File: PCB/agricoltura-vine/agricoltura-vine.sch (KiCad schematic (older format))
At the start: 0 parts

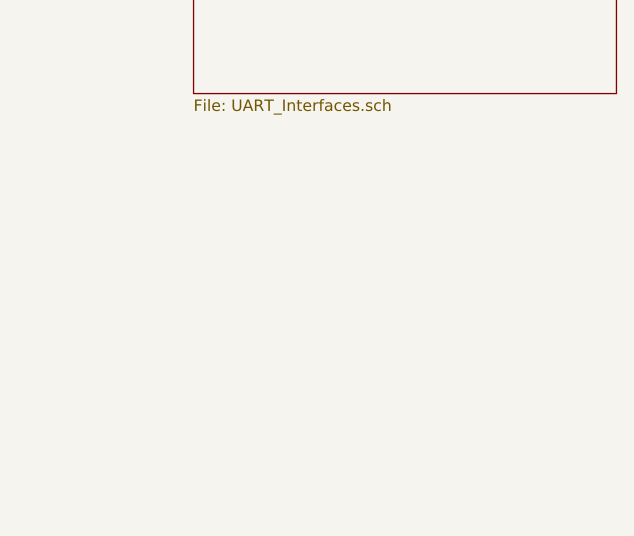
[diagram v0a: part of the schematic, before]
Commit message: 5V Logic, Connector swap, and I2C refactor
Added 5V IO logic, changed connectors over to grove style SMT, I2C refactored to use 8x mux instead fo two 4x mux.
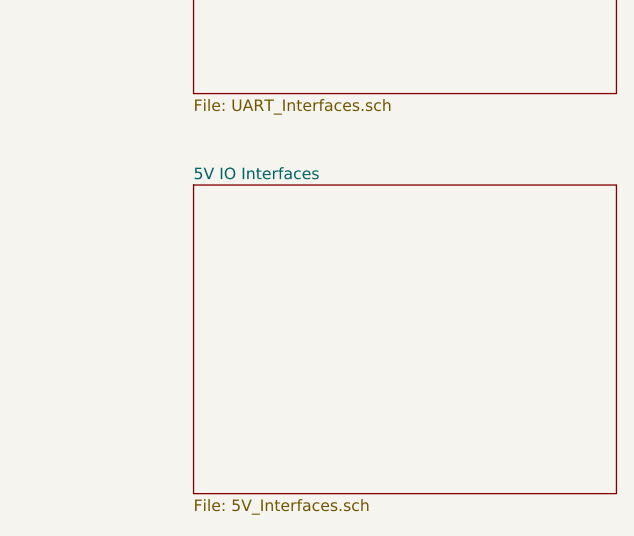
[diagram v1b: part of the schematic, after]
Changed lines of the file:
@@
 $Descr A4 11693 8268
 encoding utf-8
-Sheet 1 6
+Sheet 1 7
 Title ""
 Date ""
@@
 F1 "RS485_Interface.sch" 50
 $EndSheet
+$Sheet
+S 7550 4550 1850 1350
+U 5EF943A9
+F0 "5V IO Interfaces" 50
+F1 "5V_Interfaces.sch" 50
+$EndSheet
 $EndSCHEMATC

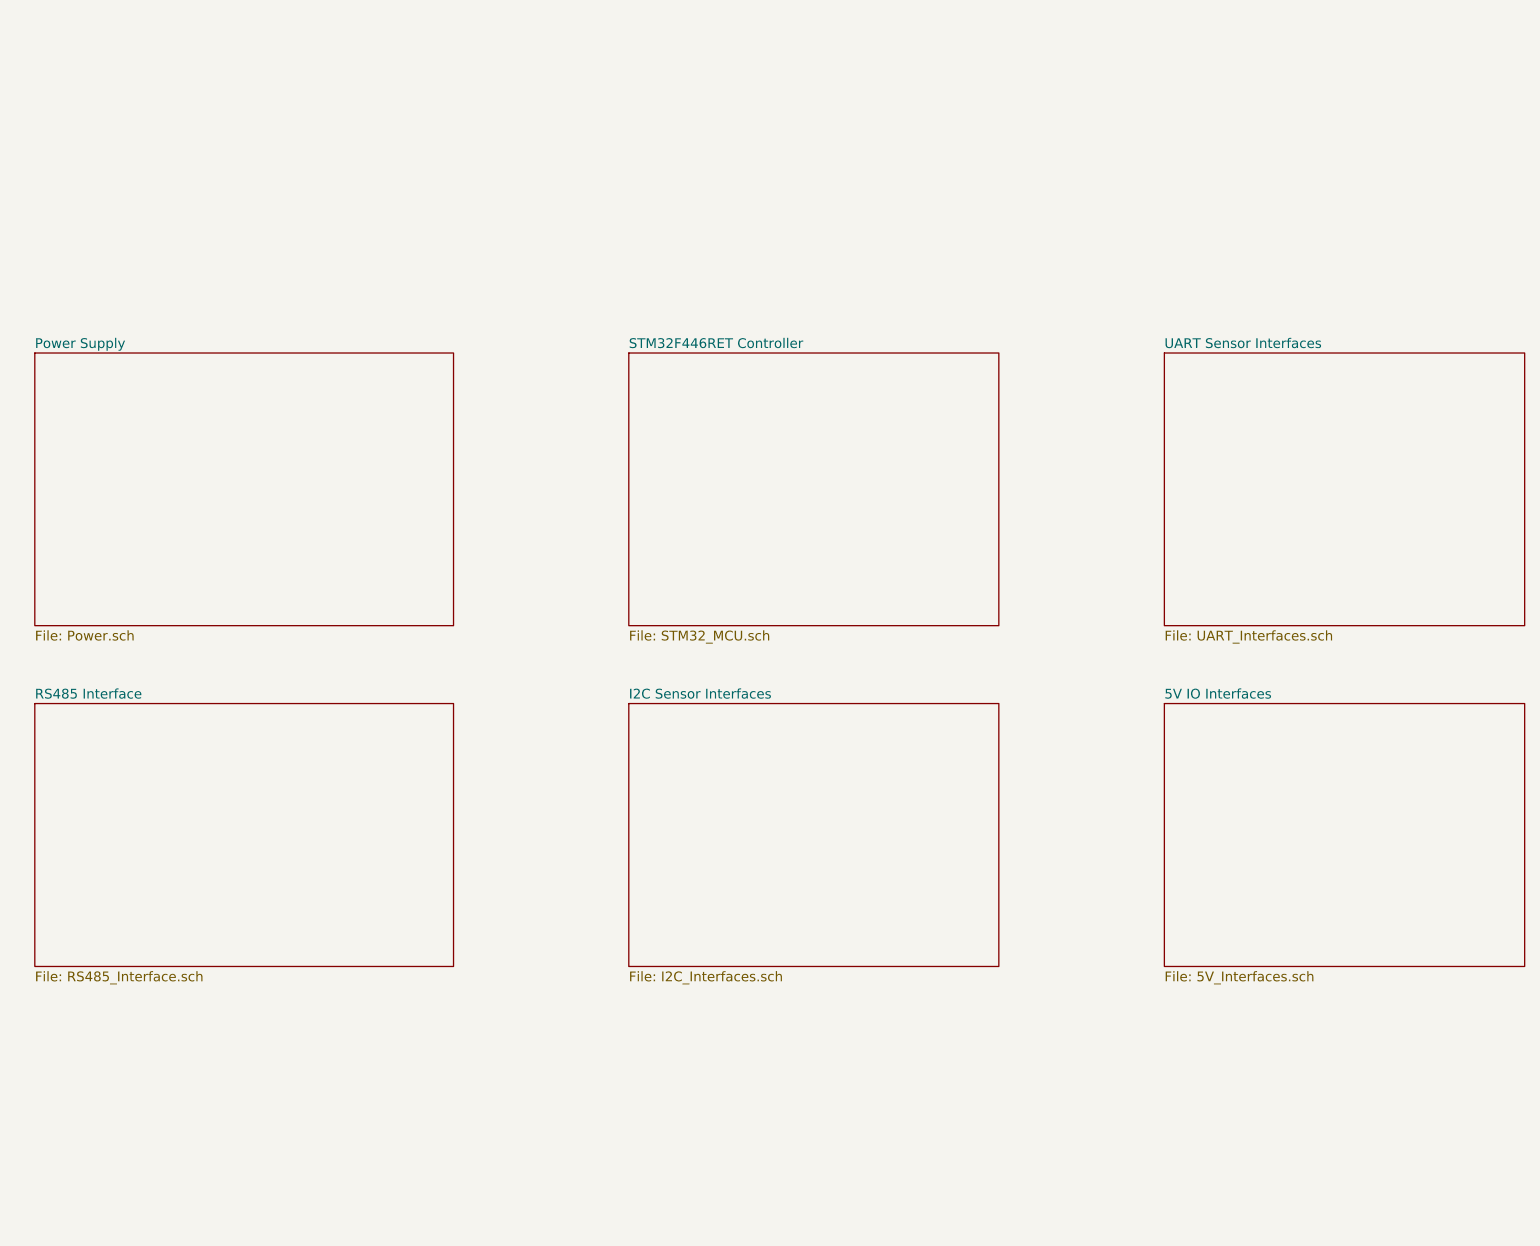
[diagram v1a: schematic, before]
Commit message: Schematic Pass 1
All subsystem schematics are completed in their first pass, some features scaled back to make design more practical.
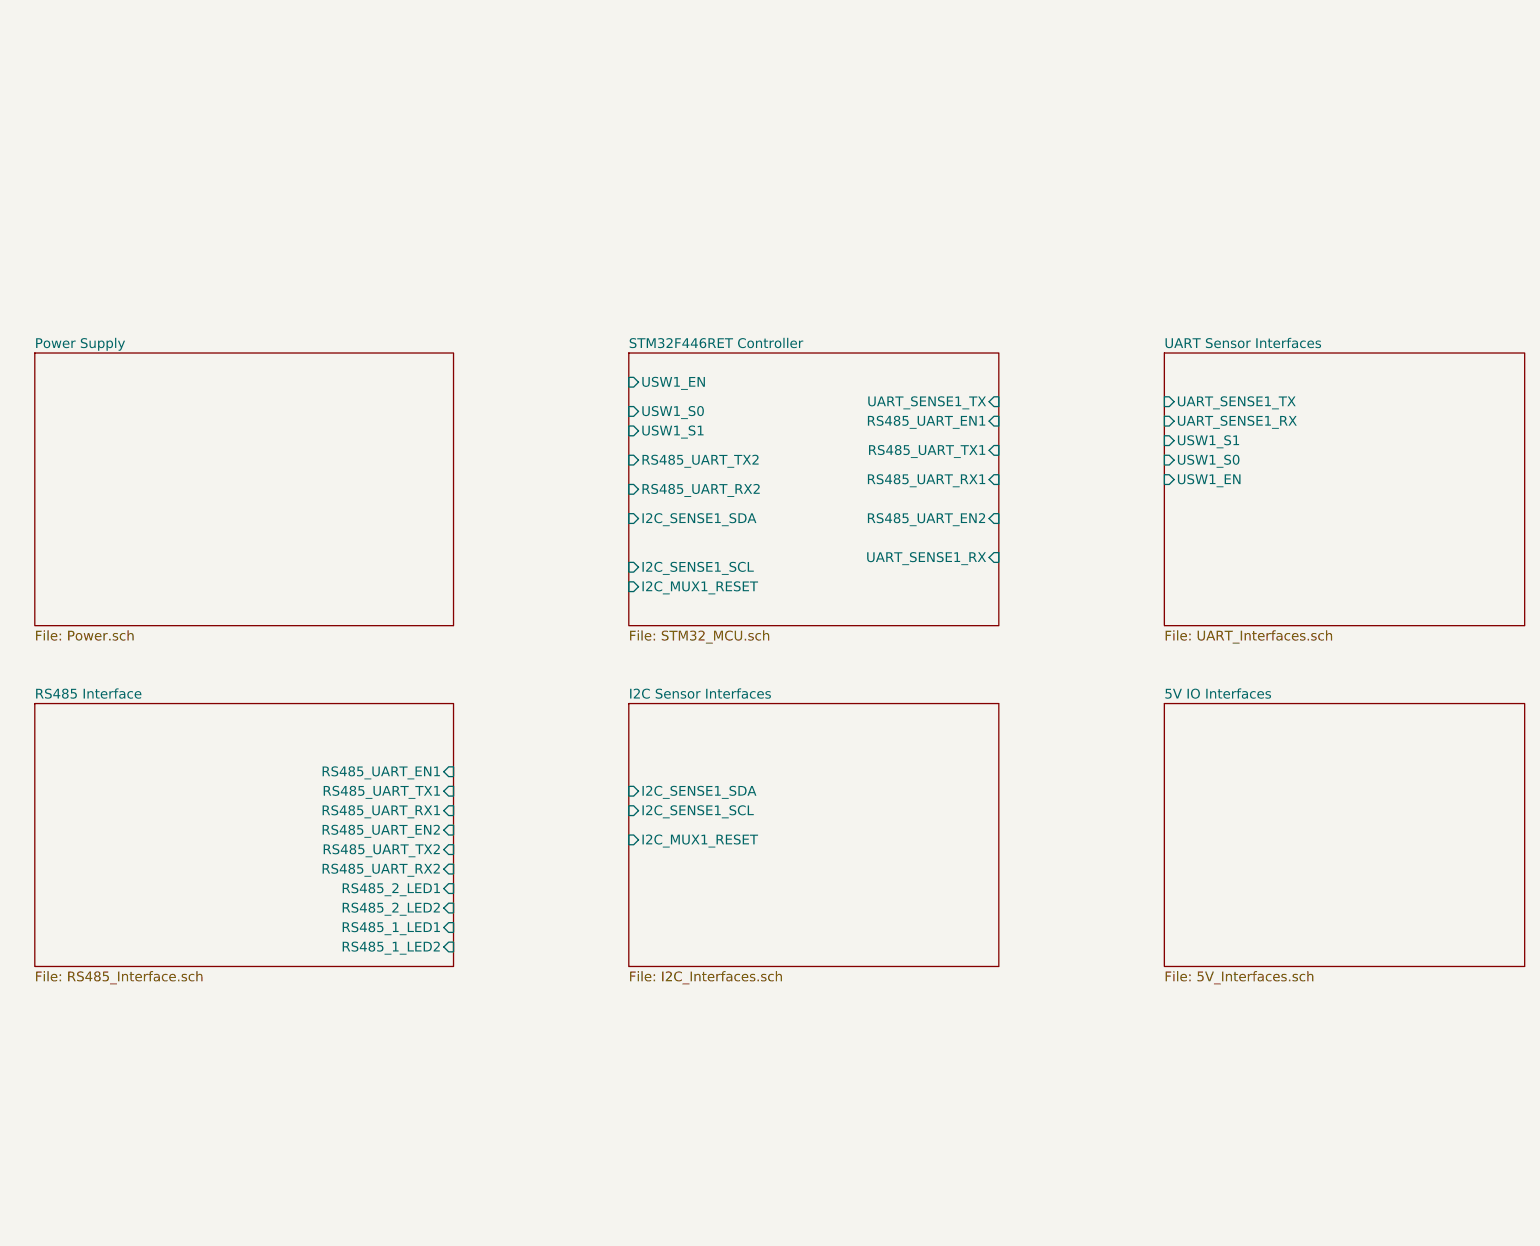
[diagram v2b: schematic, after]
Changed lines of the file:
@@
 F0 "STM32F446RET Controller" 50
 F1 "STM32_MCU.sch" 50
+F2 "UART_SENSE1_TX" I R 6700 3000 50
+F3 "RS485_UART_EN1" I R 6700 3100 50
+F4 "RS485_UART_TX1" I R 6700 3250 50
+F5 "RS485_UART_RX1" I R 6700 3400 50
+F6 "RS485_UART_EN2" I R 6700 3600 50
+F7 "RS485_UART_TX2" I L 4800 3300 50
+F8 "RS485_UART_RX2" I L 4800 3450 50
+F9 "I2C_SENSE1_SDA" I L 4800 3600 50
+F10 "I2C_SENSE1_SCL" I L 4800 3850 50
+F11 "I2C_MUX1_RESET" I L 4800 3950 50
+F12 "USW1_EN" I L 4800 2900 50
+F13 "USW1_S0" I L 4800 3050 50
+F14 "USW1_S1" I L 4800 3150 50
+F15 "UART_SENSE1_RX" I R 6700 3800 50
 $EndSheet
 $Sheet
@@
 F0 "UART Sensor Interfaces" 50
 F1 "UART_Interfaces.sch" 50
+F2 "UART_SENSE1_TX" I L 7550 3000 50
+F3 "UART_SENSE1_RX" I L 7550 3100 50
+F4 "USW1_S1" I L 7550 3200 50
+F5 "USW1_S0" I L 7550 3300 50
+F6 "USW1_EN" I L 7550 3400 50
 $EndSheet
 $Sheet
@@
 F0 "I2C Sensor Interfaces" 50
 F1 "I2C_Interfaces.sch" 50
+F2 "I2C_SENSE1_SDA" I L 4800 5000 50
+F3 "I2C_SENSE1_SCL" I L 4800 5100 50
+F4 "I2C_MUX1_RESET" I L 4800 5250 50
 $EndSheet
 $Sheet
@@
 F0 "RS485 Interface" 50
 F1 "RS485_Interface.sch" 50
+F2 "RS485_UART_EN1" I R 3900 4900 50
+F3 "RS485_UART_TX1" I R 3900 5000 50
+F4 "RS485_UART_RX1" I R 3900 5100 50
+F5 "RS485_UART_EN2" I R 3900 5200 50
+F6 "RS485_UART_TX2" I R 3900 5300 50
+F7 "RS485_UART_RX2" I R 3900 5400 50
+F8 "RS485_2_LED1" I R 3900 5500 50
+F9 "RS485_2_LED2" I R 3900 5600 50
+F10 "RS485_1_LED1" I R 3900 5700 50
+F11 "RS485_1_LED2" I R 3900 5800 50
 $EndSheet
 $Sheet

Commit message: Schematic and Readme
Readme updated with latest feature set, and schematic pages interconnected.
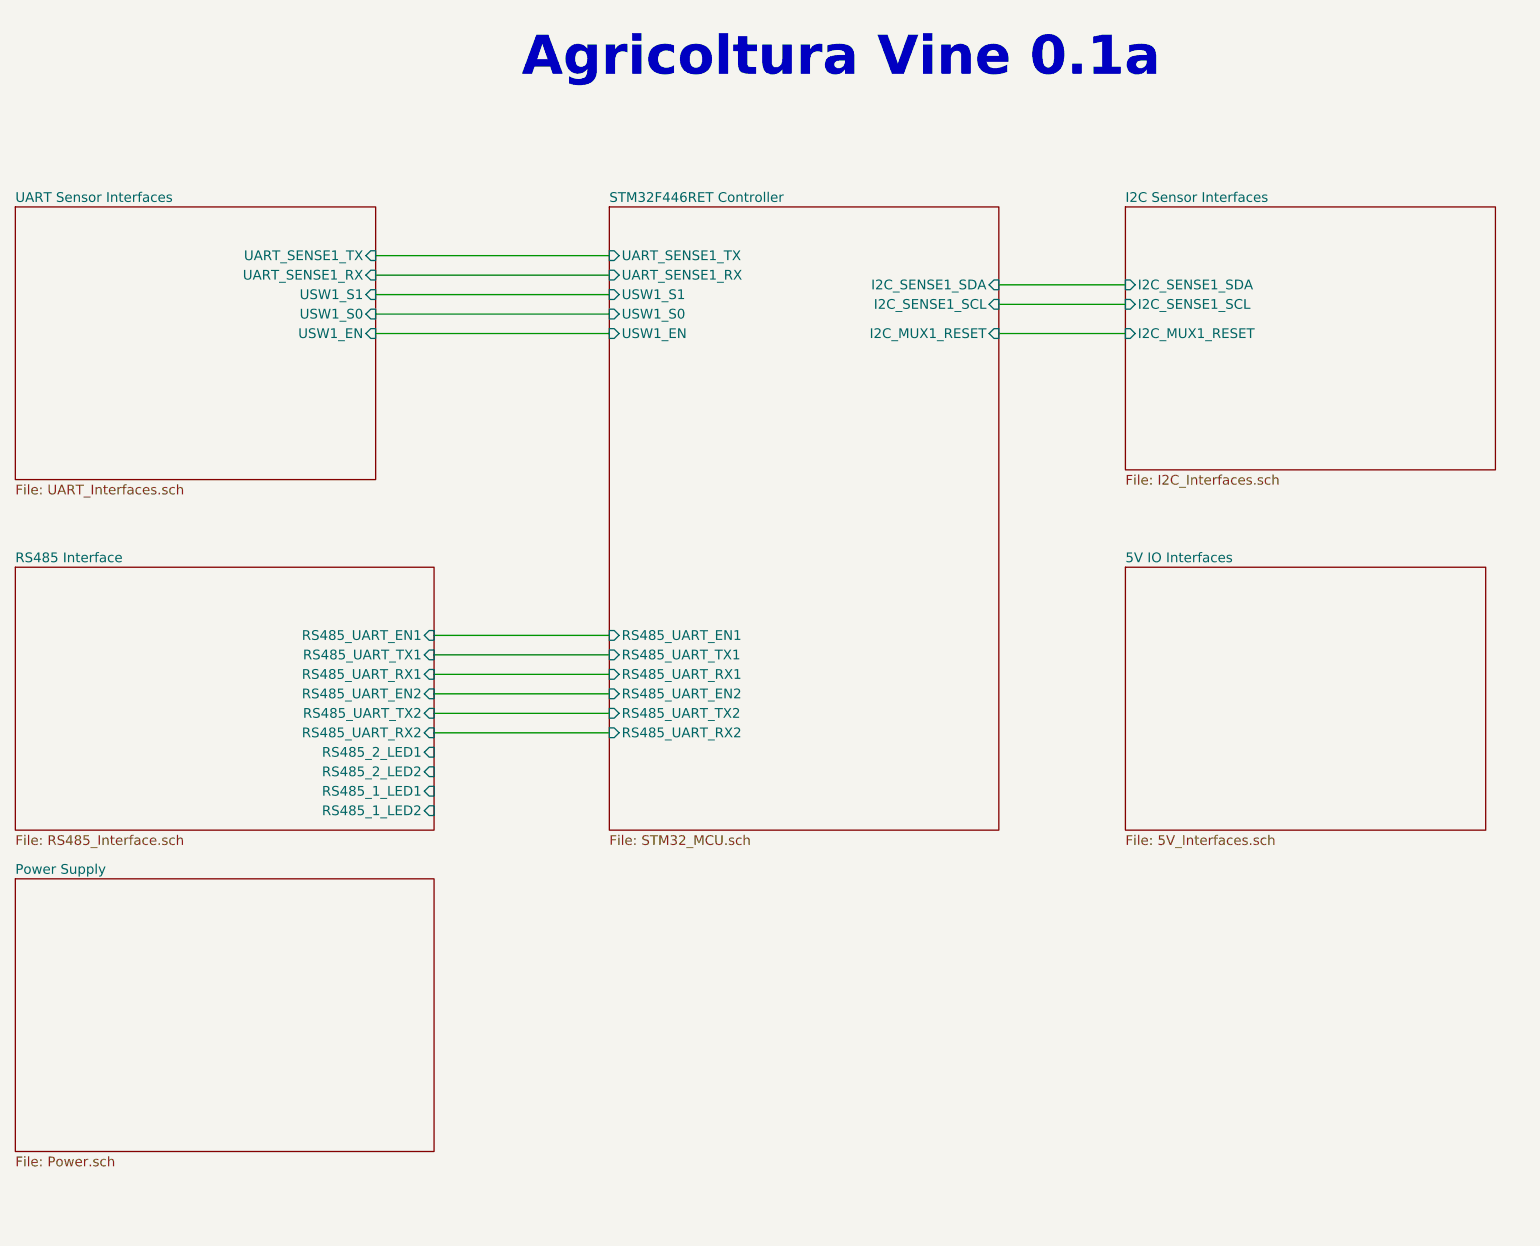
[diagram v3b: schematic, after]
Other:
- note added: "Agricoltura Vine 0.1a"
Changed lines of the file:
@@
 $EndDescr
 $Sheet
-S 4800 2750 1900 1400
+S 4700 2000 2000 3200
 U 5EE8264D
 F0 "STM32F446RET Controller" 50
 F1 "STM32_MCU.sch" 50
-F2 "UART_SENSE1_TX" I R 6700 3000 50
-F3 "RS485_UART_EN1" I R 6700 3100 50
-F4 "RS485_UART_TX1" I R 6700 3250 50
-F5 "RS485_UART_RX1" I R 6700 3400 50
-F6 "RS485_UART_EN2" I R 6700 3600 50
-F7 "RS485_UART_TX2" I L 4800 3300 50
-F8 "RS485_UART_RX2" I L 4800 3450 50
-F9 "I2C_SENSE1_SDA" I L 4800 3600 50
-F10 "I2C_SENSE1_SCL" I L 4800 3850 50
-F11 "I2C_MUX1_RESET" I L 4800 3950 50
-F12 "USW1_EN" I L 4800 2900 50
-F13 "USW1_S0" I L 4800 3050 50
-F14 "USW1_S1" I L 4800 3150 50
-F15 "UART_SENSE1_RX" I R 6700 3800 50
+F2 "UART_SENSE1_TX" I L 4700 2250 50
+F3 "RS485_UART_EN1" I L 4700 4200 50
+F4 "RS485_UART_TX1" I L 4700 4300 50
+F5 "RS485_UART_RX1" I L 4700 4400 50
+F6 "RS485_UART_EN2" I L 4700 4500 50
+F7 "RS485_UART_TX2" I L 4700 4600 50
+F8 "RS485_UART_RX2" I L 4700 4700 50
+F9 "I2C_SENSE1_SDA" I R 6700 2400 50
+F10 "I2C_SENSE1_SCL" I R 6700 2500 50
+F11 "I2C_MUX1_RESET" I R 6700 2650 50
+F12 "USW1_EN" I L 4700 2650 50
+F13 "USW1_S0" I L 4700 2550 50
+F14 "USW1_S1" I L 4700 2450 50
+F15 "UART_SENSE1_RX" I L 4700 2350 50
 $EndSheet
 $Sheet
-S 7550 2750 1850 1400
+S 1650 2000 1850 1400
 U 5EE82702
 F0 "UART Sensor Interfaces" 50
 F1 "UART_Interfaces.sch" 50
-F2 "UART_SENSE1_TX" I L 7550 3000 50
-F3 "UART_SENSE1_RX" I L 7550 3100 50
-F4 "USW1_S1" I L 7550 3200 50
-F5 "USW1_S0" I L 7550 3300 50
-F6 "USW1_EN" I L 7550 3400 50
+F2 "UART_SENSE1_TX" I R 3500 2250 50
+F3 "UART_SENSE1_RX" I R 3500 2350 50
+F4 "USW1_S1" I R 3500 2450 50
+F5 "USW1_S0" I R 3500 2550 50
+F6 "USW1_EN" I R 3500 2650 50
 $EndSheet
 $Sheet
-S 4800 4550 1900 1350
+S 7350 2000 1900 1350
 U 5EE827B2
 F0 "I2C Sensor Interfaces" 50
 F1 "I2C_Interfaces.sch" 50
-F2 "I2C_SENSE1_SDA" I L 4800 5000 50
-F3 "I2C_SENSE1_SCL" I L 4800 5100 50
-F4 "I2C_MUX1_RESET" I L 4800 5250 50
+F2 "I2C_SENSE1_SDA" I L 7350 2400 50
+F3 "I2C_SENSE1_SCL" I L 7350 2500 50
+F4 "I2C_MUX1_RESET" I L 7350 2650 50
 $EndSheet
 $Sheet
-S 1750 2750 2150 1400
+S 1650 5450 2150 1400
 U 5EE8280D
 F0 "Power Supply" 50
@@
 $EndSheet
 $Sheet
-S 1750 4550 2150 1350
+S 1650 3850 2150 1350
 U 5EE82896
 F0 "RS485 Interface" 50
 F1 "RS485_Interface.sch" 50
-F2 "RS485_UART_EN1" I R 3900 4900 50
-F3 "RS485_UART_TX1" I R 3900 5000 50
-F4 "RS485_UART_RX1" I R 3900 5100 50
-F5 "RS485_UART_EN2" I R 3900 5200 50
-F6 "RS485_UART_TX2" I R 3900 5300 50
-F7 "RS485_UART_RX2" I R 3900 5400 50
-F8 "RS485_2_LED1" I R 3900 5500 50
-F9 "RS485_2_LED2" I R 3900 5600 50
-F10 "RS485_1_LED1" I R 3900 5700 50
-F11 "RS485_1_LED2" I R 3900 5800 50
+F2 "RS485_UART_EN1" I R 3800 4200 50
+F3 "RS485_UART_TX1" I R 3800 4300 50
+F4 "RS485_UART_RX1" I R 3800 4400 50
+F5 "RS485_UART_EN2" I R 3800 4500 50
+F6 "RS485_UART_TX2" I R 3800 4600 50
+F7 "RS485_UART_RX2" I R 3800 4700 50
+F8 "RS485_2_LED1" I R 3800 4800 50
+F9 "RS485_2_LED2" I R 3800 4900 50
+F10 "RS485_1_LED1" I R 3800 5000 50
+F11 "RS485_1_LED2" I R 3800 5100 50
 $EndSheet
 $Sheet
-S 7550 4550 1850 1350
+S 7350 3850 1850 1350
 U 5EF943A9
 F0 "5V IO Interfaces" 50
 F1 "5V_Interfaces.sch" 50
 $EndSheet
+Wire Wire Line
+	3800 4200 4700 4200
+Wire Wire Line
+	3800 4300 4700 4300
+Wire Wire Line
+	4700 4400 3800 4400
+Wire Wire Line
+	3800 4500 4700 4500
+Wire Wire Line
+	4700 4600 3800 4600
+Wire Wire Line
+	3800 4700 4700 4700
+Wire Wire Line
+	7350 2650 6700 2650
+Wire Wire Line
+	6700 2500 7350 2500
+Wire Wire Line
+	6700 2400 7350 2400
+Wire Wire Line
+	3500 2350 4700 2350
+Wire Wire Line
+	3500 2250 4700 2250
+Wire Wire Line
+	4700 2450 3500 2450
+Wire Wire Line
+	3500 2550 4700 2550
+Wire Wire Line
+	4700 2650 3500 2650
+Text Notes 4250 1350 0    200  ~ 40
+Agricoltura Vine 0.1a
 $EndSCHEMATC
